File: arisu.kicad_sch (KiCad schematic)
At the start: 8 parts

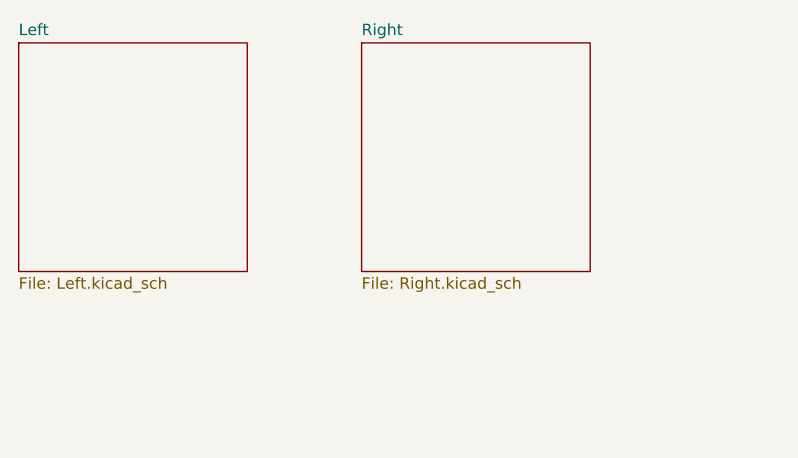
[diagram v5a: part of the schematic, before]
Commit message: Hot pluggable trrs
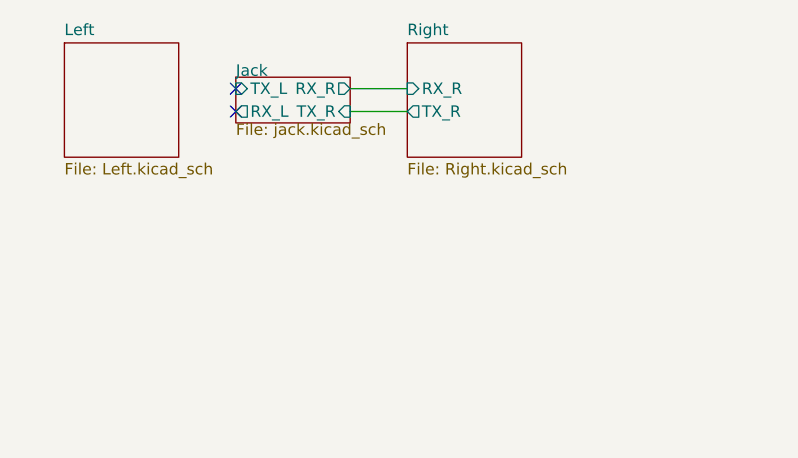
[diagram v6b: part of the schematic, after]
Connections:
- no-connect marks 0 -> 2
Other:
- added sheet Jack (jack.kicad_sch)
- sheet Right ports: added RX_R, TX_R; removed none

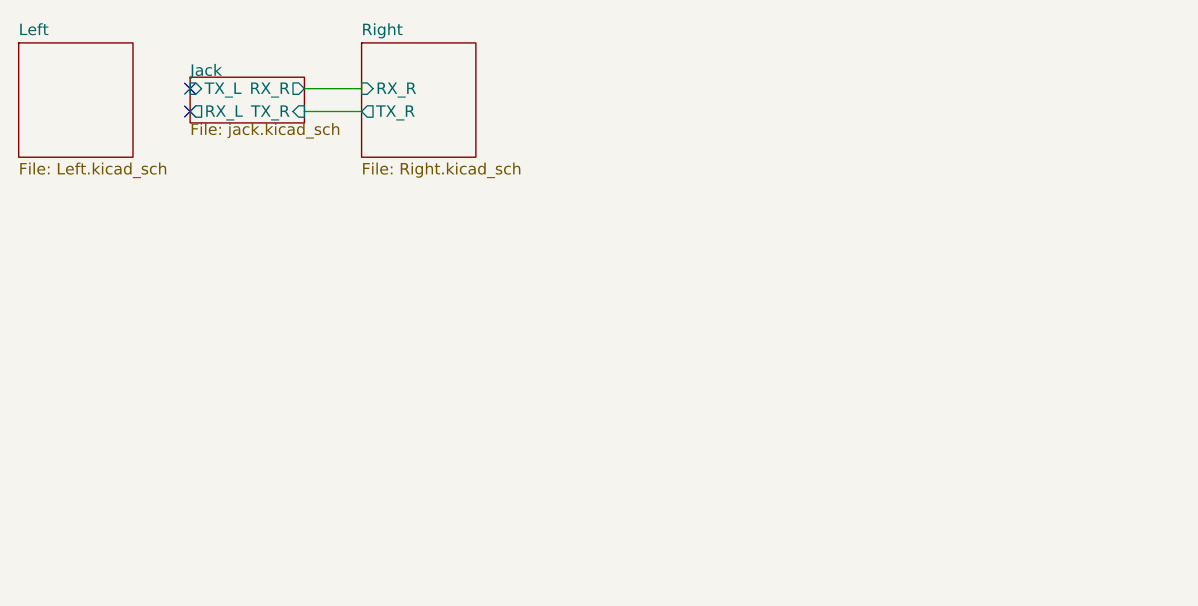
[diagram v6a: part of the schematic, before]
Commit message: No more erc errors + centering and socketing of switches
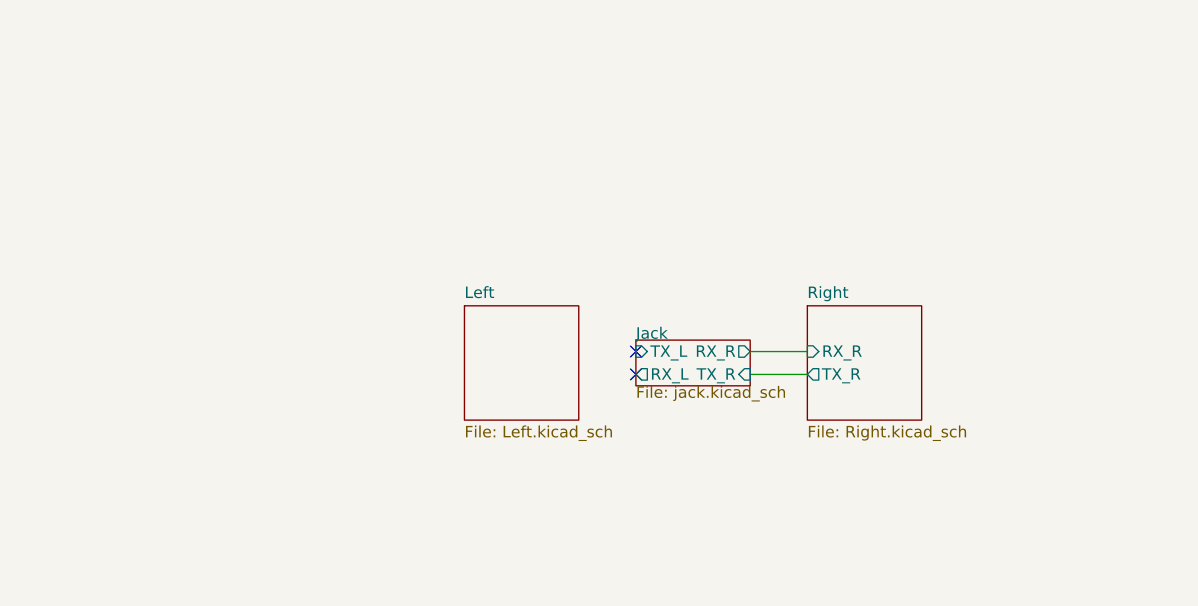
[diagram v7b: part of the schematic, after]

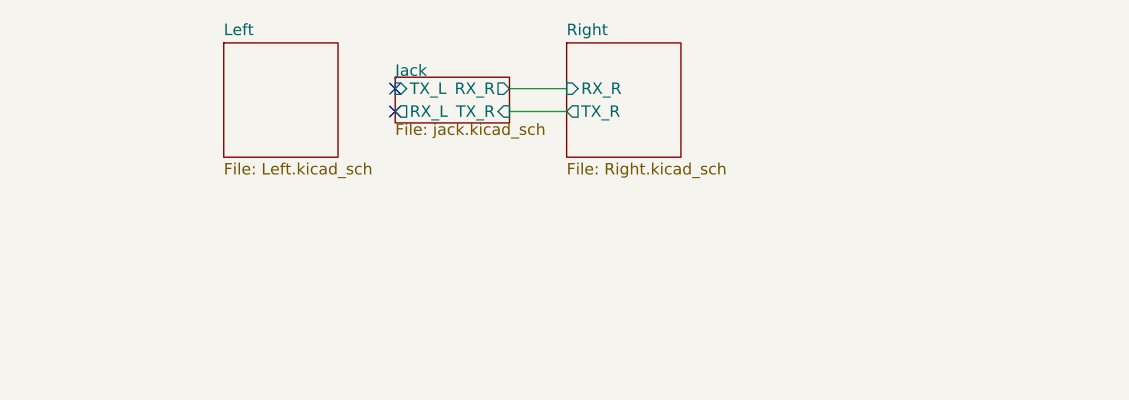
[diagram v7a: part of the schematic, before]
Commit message: Add second micro back in, and added some footprints
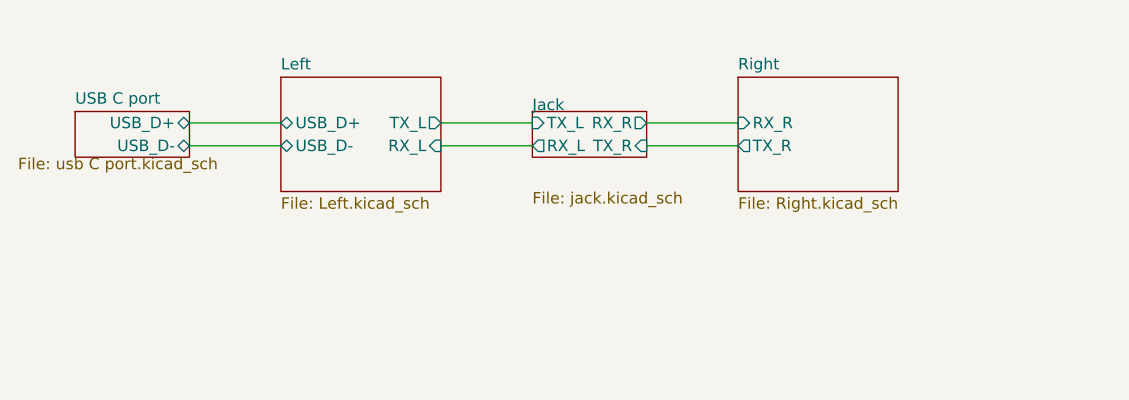
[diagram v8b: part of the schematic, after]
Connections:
- no-connect marks 2 -> 0
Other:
- added sheet USB C port (usb C port.kicad_sch)
- sheet Left ports: added RX_L, TX_L, USB_D+, USB_D-; removed none
